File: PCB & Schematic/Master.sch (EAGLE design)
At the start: 3 parts

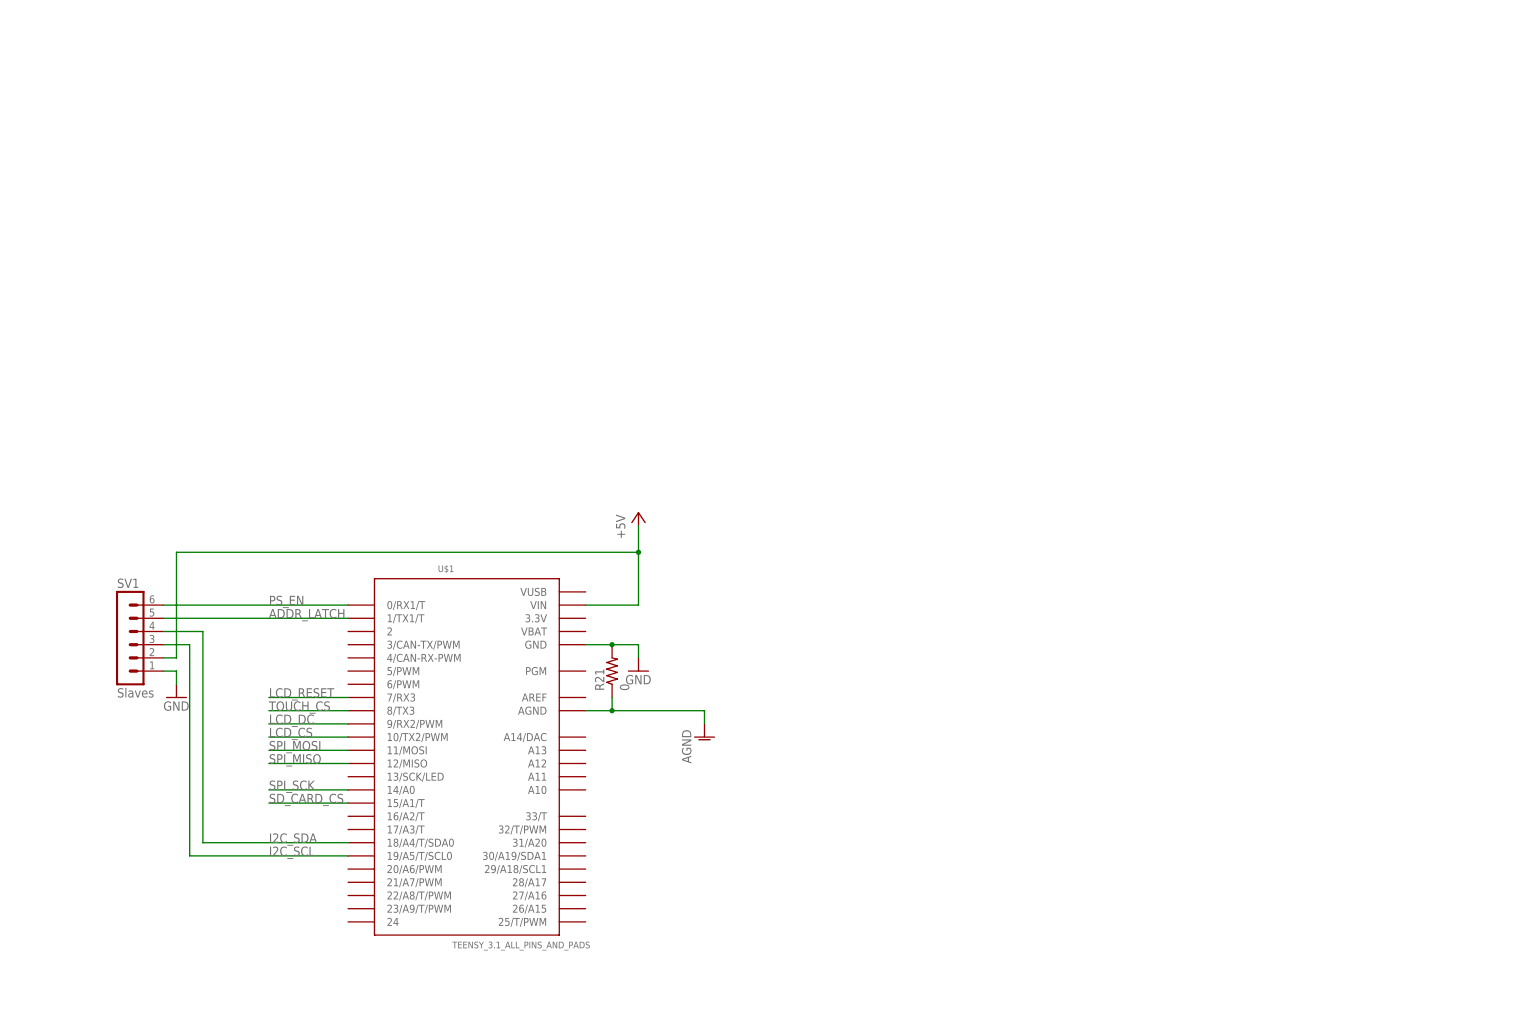
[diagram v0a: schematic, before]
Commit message: Get started adding DIN MIDI In/Out plugs.
I need to get parts in and test this.
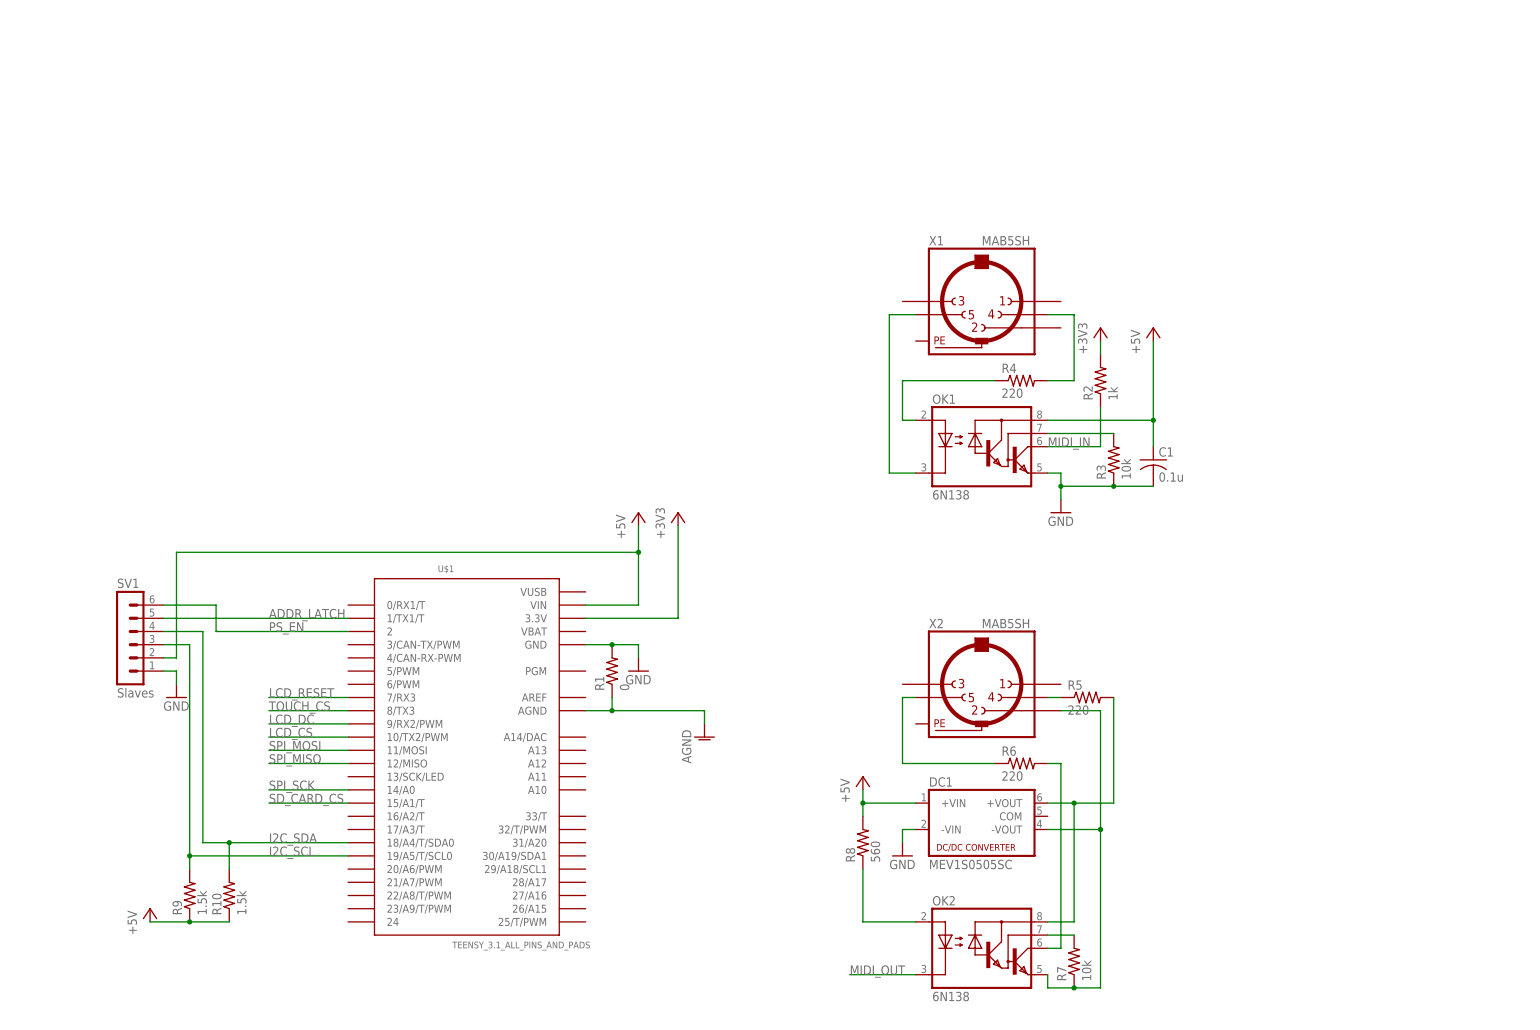
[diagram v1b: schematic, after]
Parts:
- added C1: 0.1u, resistor:C-USC0805
- added DC1: MEV1S0505SC, dc-dc-converter:NMA
- added OK1, OK2: 6N138, optocoupler:6N138
- added R10, R9: 1.5k, resistor:R-US_R0805
- added R2: 1k, resistor:R-US_R0805
- added R3, R7: 10k, resistor:R-US_R0805
- added R4, R5, R6: 220, resistor:R-US_R0805
- added R8: 560, resistor:R-US_R0805
- added X1, X2: MAB5SH, con-hirschmann:MAB5SH
- renumbered R21 to R1
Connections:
- new net +3V3: R2.2, U$1.3.3V
- new net MIDI_IN: OK1.VO, R2.1
- new net MIDI_OUT: OK2.C
- new net N$1: R6.1, X2.5
- new net N$10: OK2.VB, R7.2
- new net N$11: DC1.-VOUT, OK2.GND, R7.1, X2.2
- new net N$2: OK1.VB, R3.2
- new net N$3: OK1.A, R4.1
- new net N$4: R4.2, X1.4
- new net N$5: OK1.C, X1.5
- new net N$6: OK2.VO, R6.2
- new net N$7: R5.1, X2.4
- new net N$8: DC1.+VOUT, OK2.VCC, R5.2
- new net N$9: OK2.A, R8.1
- net +5V: now also C1.1, DC1.+VIN, OK1.VCC, R10.1, R8.2, R9.1
- net GND: now also C1.2, DC1.-VIN, OK1.GND, R3.1
- net I2C_SCL: now also R9.2
- net I2C_SDA: now also R10.2
- net PS_EN: now also U$1.2; no longer U$1.0/RX1/T

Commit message: Finish physical MIDI schematic, initial firmware.
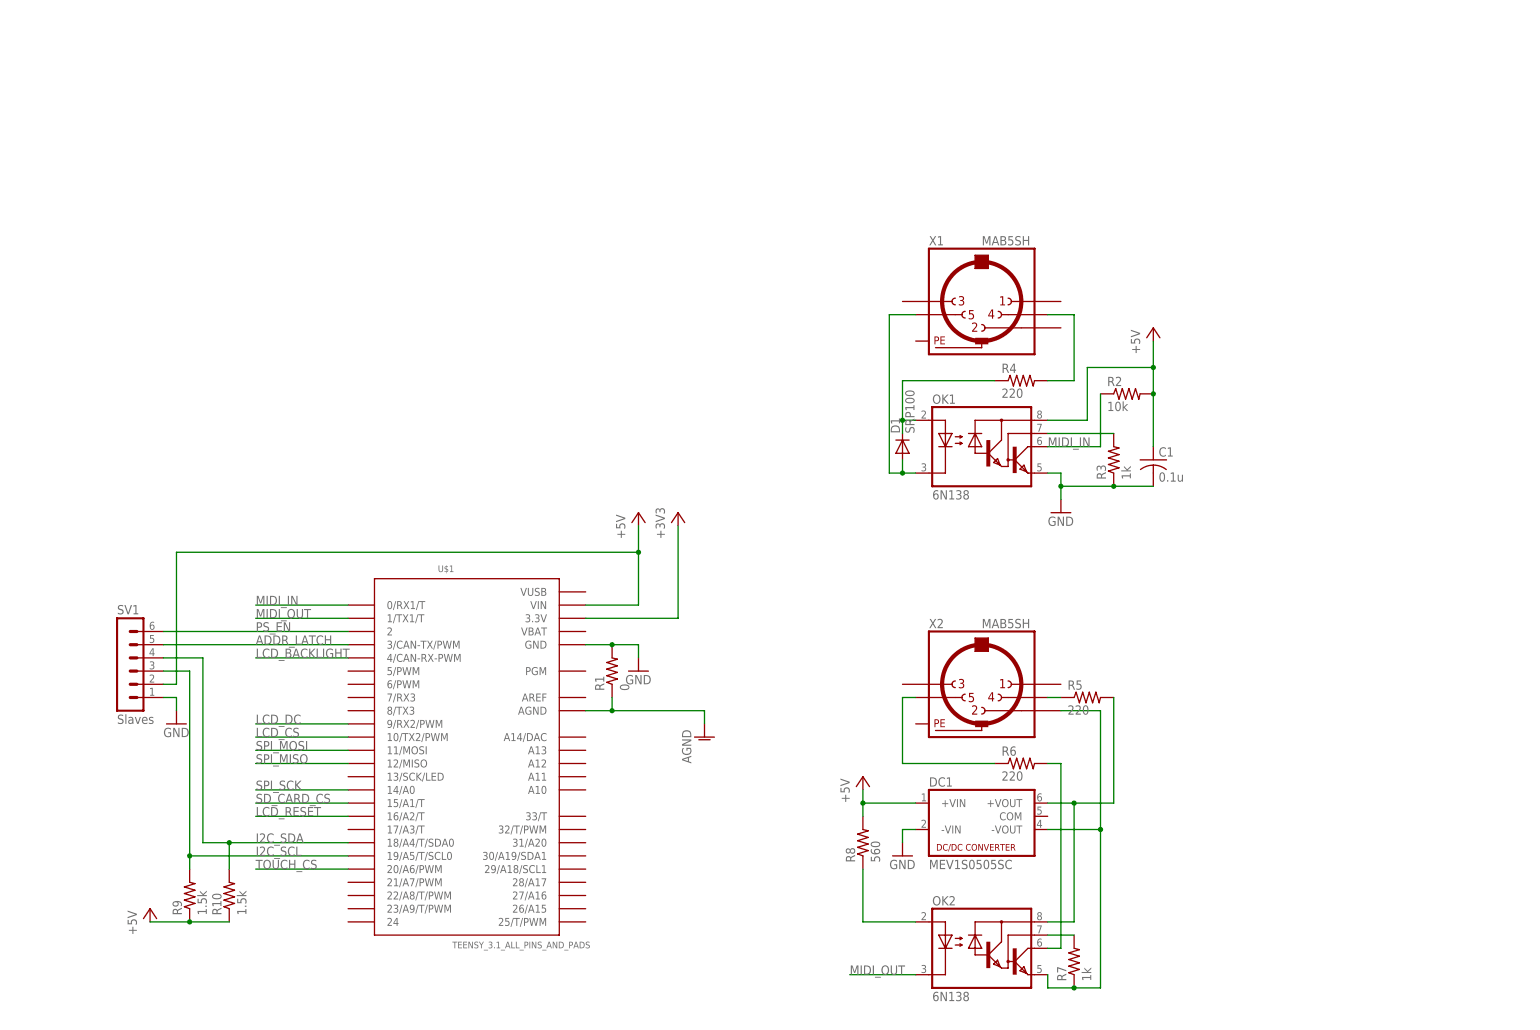
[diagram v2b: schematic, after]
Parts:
- added D1: SRP100, diode:SRP100
- R2: value 1k -> 10k
- R3, R7: value 10k -> 1k
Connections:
- new net LCD_BACKLIGHT: U$1.4/CAN-RX-PWM
- net +3V3: no longer R2.2
- net +5V: now also R2.2
- net ADDR_LATCH: now also U$1.3/CAN-TX/PWM; no longer U$1.1/TX1/T
- net LCD_RESET: now also U$1.16/A2/T; no longer U$1.7/RX3
- net MIDI_IN: now also U$1.0/RX1/T
- net MIDI_OUT: now also U$1.1/TX1/T
- net N$3: now also D1.C
- net N$5: now also D1.A
- net TOUCH_CS: now also U$1.20/A6/PWM; no longer U$1.8/TX3
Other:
- moved on the sheet: R2, SV1

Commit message: Begin PCB for the master. Missing key features!
It is missing the power supply connector, among other things.
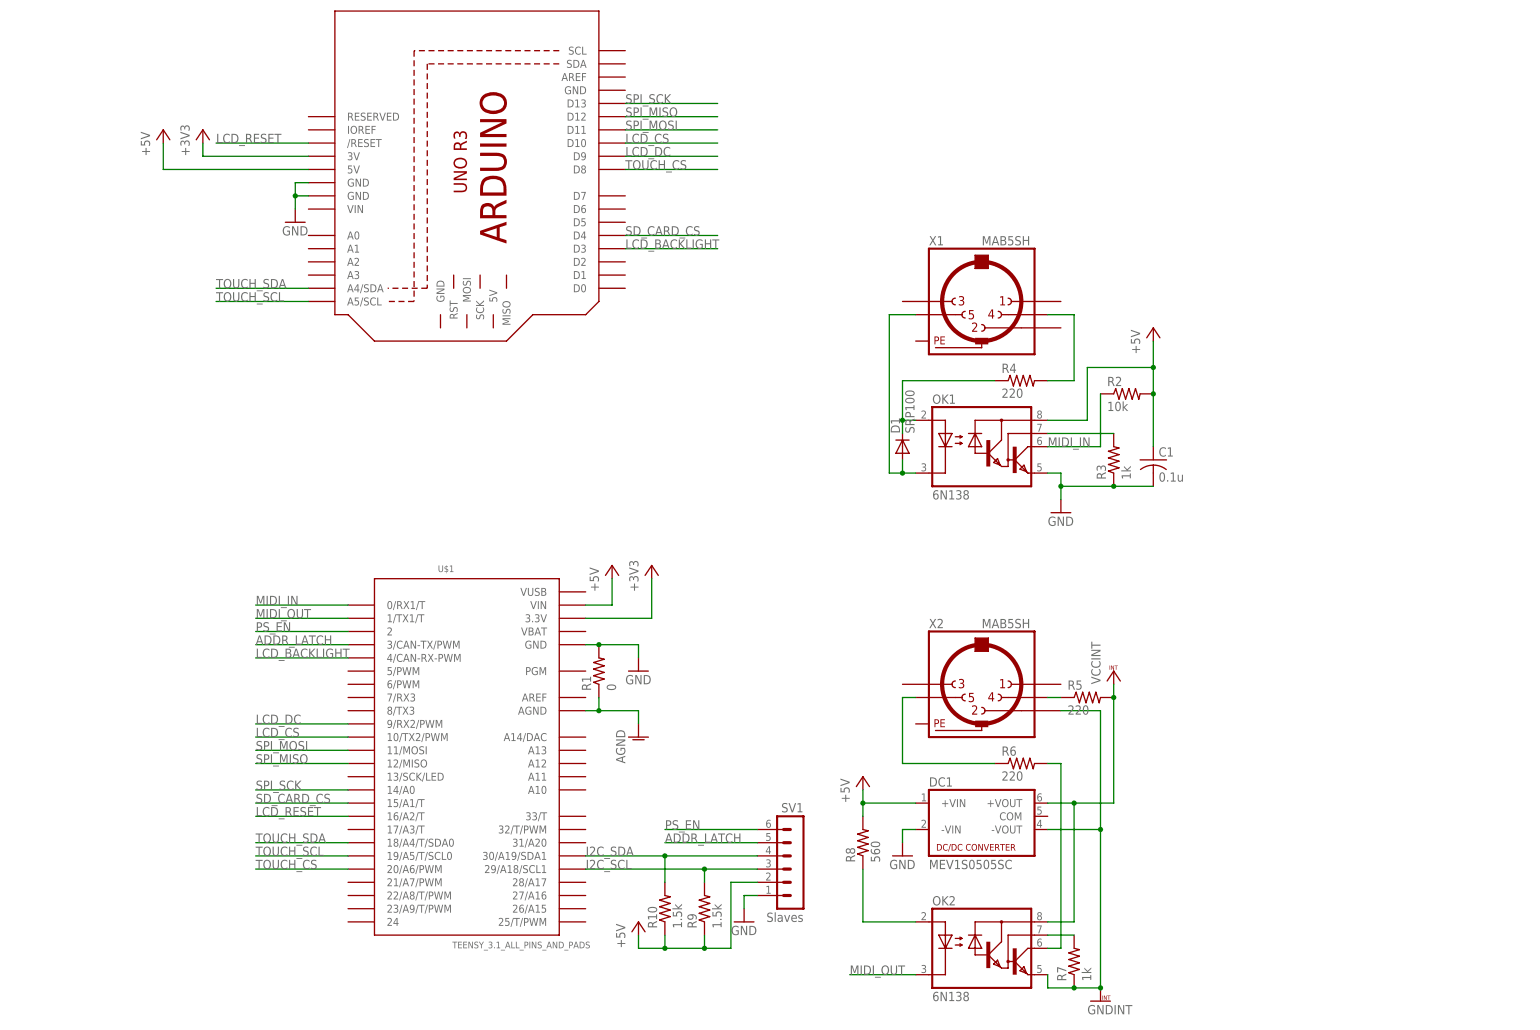
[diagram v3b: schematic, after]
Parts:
- added M1: ARDUINO_R3_ICSP_NODIM, adafruit:ARDUINO_R3_ICSP_NODIM
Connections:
- net N$11 renamed GNDINT
- net N$8 renamed VCCINT
- new net TOUCH_SCL: M1.A5/SCL, U$1.19/A5/T/SCL0
- new net TOUCH_SDA: M1.A4/SDA, U$1.18/A4/T/SDA0
- net +3V3: now also M1.3V
- net +5V: now also M1.5V
- net GND: now also M1.GND@1, M1.GND@2
- net I2C_SCL: now also U$1.29/A18/SCL1; no longer U$1.19/A5/T/SCL0
- net I2C_SDA: now also U$1.30/A19/SDA1; no longer U$1.18/A4/T/SDA0
- net LCD_BACKLIGHT: now also M1.D3
- net LCD_CS: now also M1.D10
- net LCD_DC: now also M1.D9
- net LCD_RESET: now also M1./RESET
- net SD_CARD_CS: now also M1.D4
- net SPI_MISO: now also M1.D12
- net SPI_MOSI: now also M1.D11
- net SPI_SCK: now also M1.D13
- net TOUCH_CS: now also M1.D8
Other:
- moved on the sheet: R1, R10, R9, SV1

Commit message: Finish master PCB layout.
I should verify the watchdog and power supply work as claimed
before ordering a PCB, though.
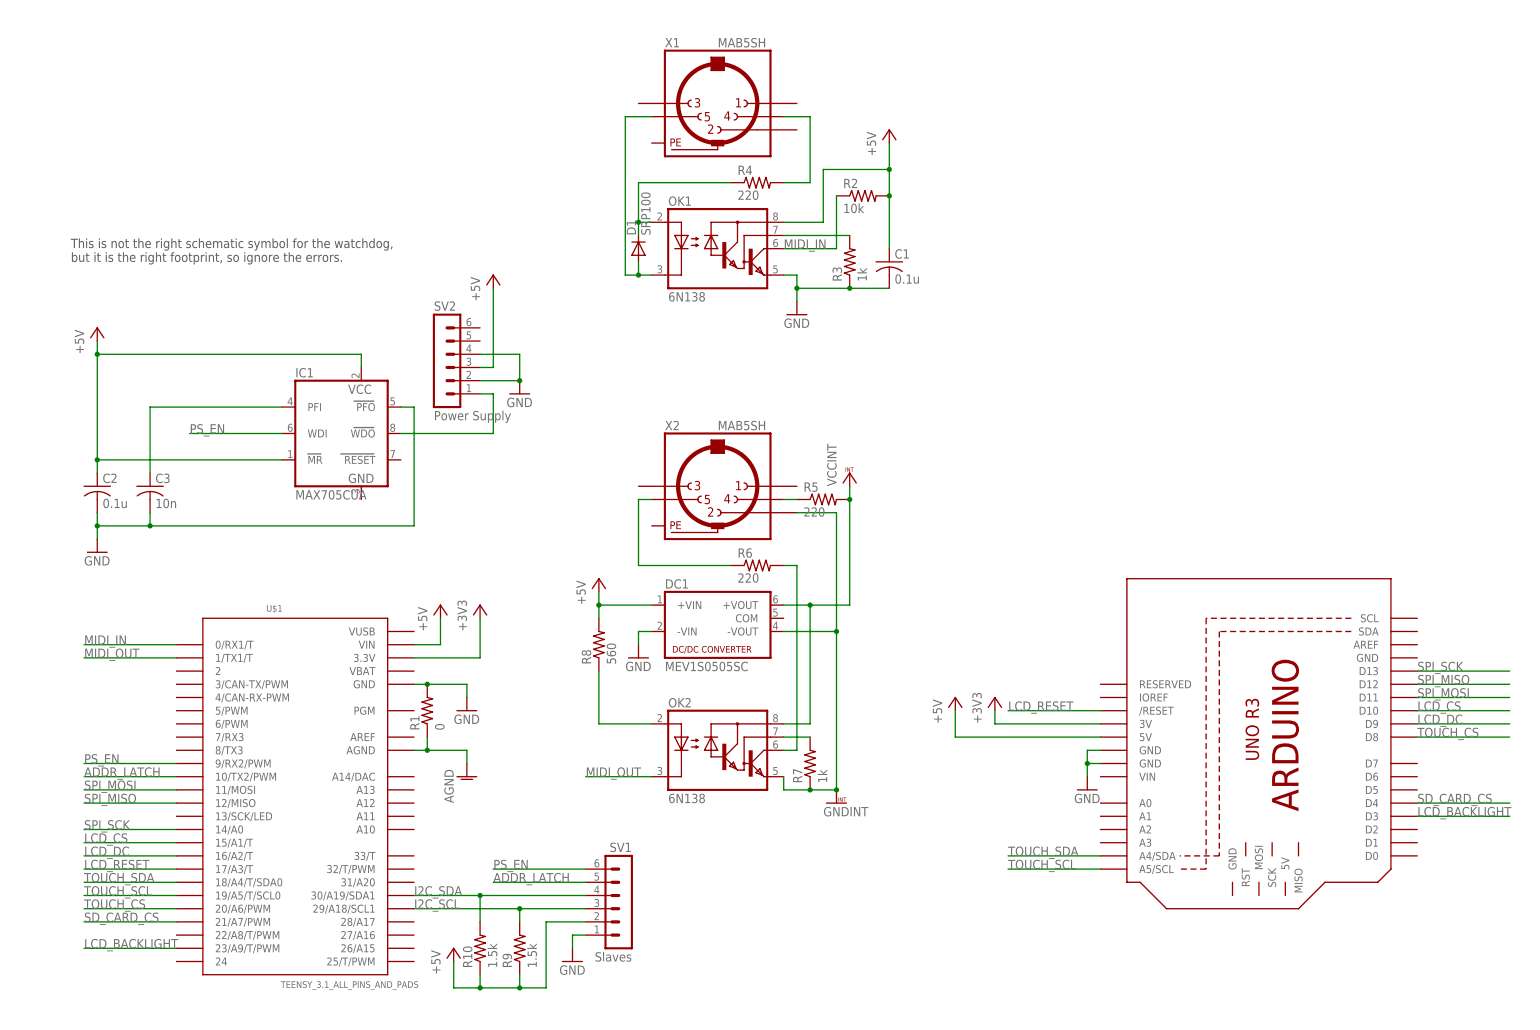
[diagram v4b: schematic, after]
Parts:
- added C2: 0.1u, resistor:C-USC0805
- added C3: 10n, resistor:C-USC0805
- added IC1: MAX705CUA, maxim:MAX705CUA
- added SV2: Power Supply, con-lstb:MA06-1
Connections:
- new net N$11: IC1.WDO, SV2.1
- new net N$15: C3.1, IC1.PFI
- net +5V: now also C2.1, IC1.MR, IC1.VCC, SV2.3
- net ADDR_LATCH: now also U$1.10/TX2/PWM; no longer U$1.3/CAN-TX/PWM
- net GND: now also C2.2, C3.2, IC1.PFO, SV2.2, SV2.4
- net LCD_BACKLIGHT: now also U$1.23/A9/T/PWM; no longer U$1.4/CAN-RX-PWM
- net LCD_CS: now also U$1.15/A1/T; no longer U$1.10/TX2/PWM
- net LCD_DC: now also U$1.16/A2/T; no longer U$1.9/RX2/PWM
- net LCD_RESET: now also U$1.17/A3/T; no longer U$1.16/A2/T
- net PS_EN: now also IC1.WDI, U$1.9/RX2/PWM; no longer U$1.2
- net SD_CARD_CS: now also U$1.21/A7/PWM; no longer U$1.15/A1/T
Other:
- note added: "This is not the right schematic symbol for the watchdog, but it is the right footprint, so ignore the errors."
- moved on the sheet: C1, D1, DC1, OK1, OK2, R1, R10, R2, R3, R4, R5, R6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
